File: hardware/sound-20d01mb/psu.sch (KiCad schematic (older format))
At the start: 14 parts

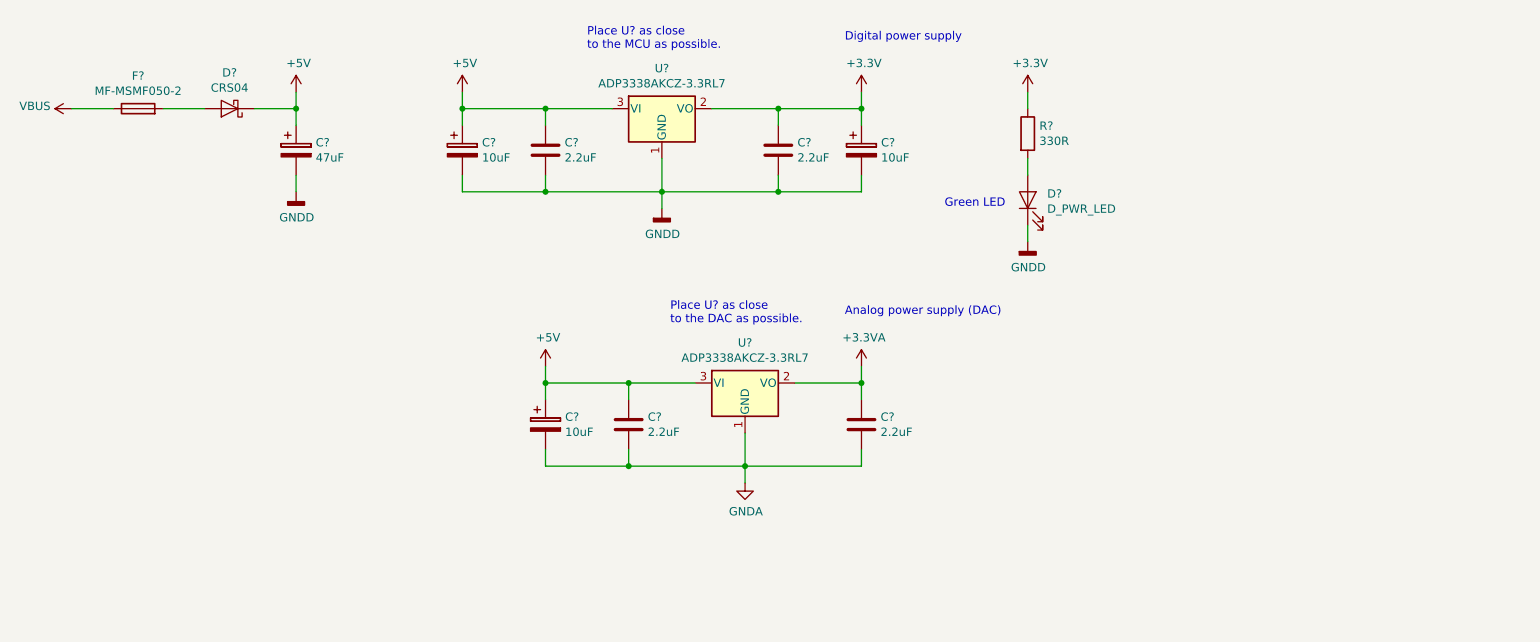
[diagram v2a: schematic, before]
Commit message: Connected GNDD and GNDA
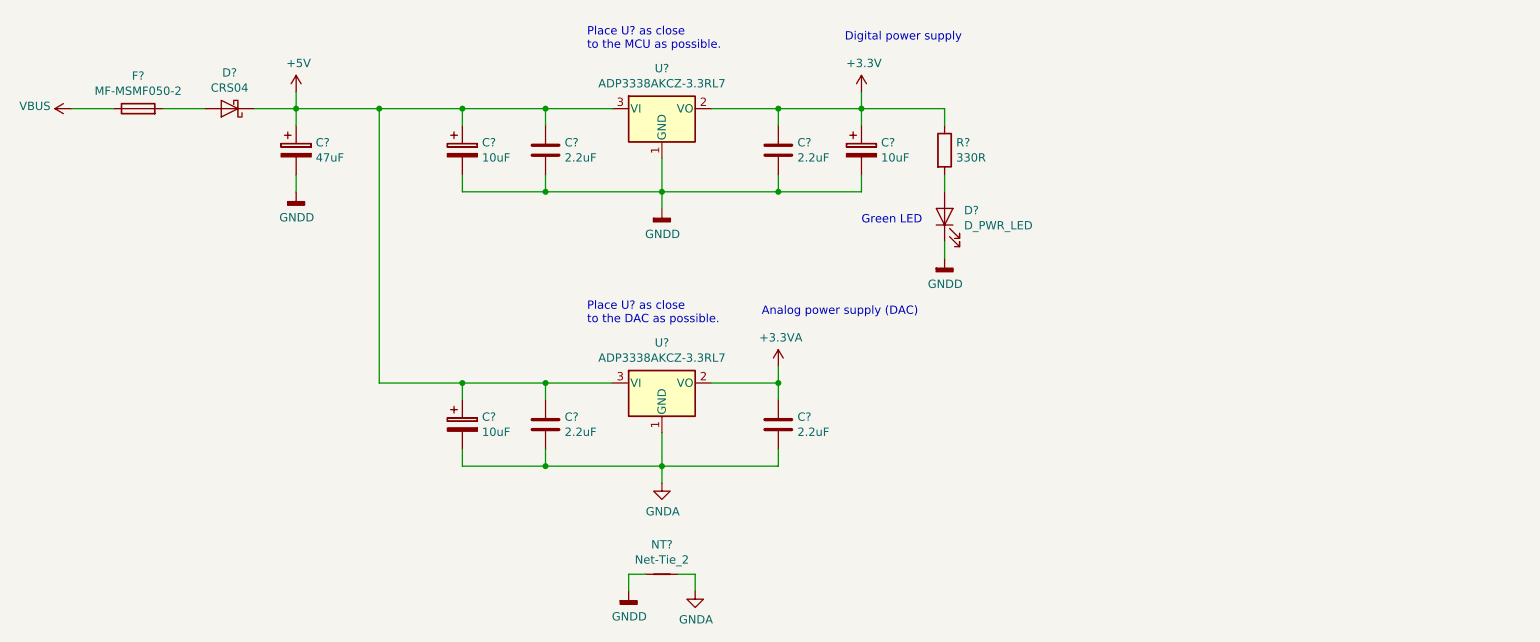
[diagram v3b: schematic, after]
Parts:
- added NT?: Net-Tie_2, NetTie:NetTie-2_SMD_Pad2.0mm, symbol Device:Net-Tie_2
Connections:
- net GNDA: now also NT?.2
- net GNDD: now also NT?.1
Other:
- moved on the sheet: C?, D?, R?, U?
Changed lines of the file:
@@
 L Regulator_Linear:AZ1117-3.3 U?
 U 1 1 60DF628F
-P 6150 4450
-F 0 "U?" H 6150 4692 50  0000 C CNN
-F 1 "ADP3338AKCZ-3.3RL7" H 6150 4601 50  0000 C CNN
-F 2 "Package_TO_SOT_SMD:SOT-223-3_TabPin2" H 6150 4700 50  0001 C CIN
-F 3 "https://www.analog.com/media/en/technical-documentation/data-sheets/adp3338.pdf" H 6150 4450 50  0001 C CNN
-	1    6150 4450
+P 5650 4450
+F 0 "U?" H 5650 4692 50  0000 C CNN
+F 1 "ADP3338AKCZ-3.3RL7" H 5650 4601 50  0000 C CNN
+F 2 "Package_TO_SOT_SMD:SOT-223-3_TabPin2" H 5650 4700 50  0001 C CIN
+F 3 "https://www.analog.com/media/en/technical-documentation/data-sheets/adp3338.pdf" H 5650 4450 50  0001 C CNN
+	1    5650 4450
 	1    0    0    -1
 $EndComp
@@
 L Device:C C?
 U 1 1 60E015B2
-P 6850 4700
+P 6350 4700
 AR Path="/60DE2DF4/60E015B2" Ref="C?"  Part="1"
 AR Path="/60DE2DF1/60E015B2" Ref="C?"  Part="1"
 AR Path="/61033008/60E015B2" Ref="C?"  Part="1"
-F 0 "C?" H 6965 4746 50  0000 L CNN
-F 1 "2.2uF" H 6965 4655 50  0000 L CNN
-F 2 "Capacitor_SMD:C_1206_3216Metric_Pad1.42x1.75mm_HandSolder" H 6888 4550 50  0001 C CNN
-F 3 "~" H 6850 4700 50  0001 C CNN
-	1    6850 4700
+F 0 "C?" H 6465 4746 50  0000 L CNN
+F 1 "2.2uF" H 6465 4655 50  0000 L CNN
+F 2 "Capacitor_SMD:C_1206_3216Metric_Pad1.42x1.75mm_HandSolder" H 6388 4550 50  0001 C CNN
+F 3 "~" H 6350 4700 50  0001 C CNN
+	1    6350 4700
 	1    0    0    -1
 $EndComp
@@
 L Device:C C?
 U 1 1 60E01602
-P 5450 4700
+P 4950 4700
 AR Path="/60DE2DF4/60E01602" Ref="C?"  Part="1"
 AR Path="/60DE2DF1/60E01602" Ref="C?"  Part="1"
 AR Path="/61033008/60E01602" Ref="C?"  Part="1"
-F 0 "C?" H 5565 4746 50  0000 L CNN
-F 1 "2.2uF" H 5565 4655 50  0000 L CNN
-F 2 "Capacitor_SMD:C_1206_3216Metric_Pad1.42x1.75mm_HandSolder" H 5488 4550 50  0001 C CNN
-F 3 "~" H 5450 4700 50  0001 C CNN
-	1    5450 4700
+F 0 "C?" H 5065 4746 50  0000 L CNN
+F 1 "2.2uF" H 5065 4655 50  0000 L CNN
+F 2 "Capacitor_SMD:C_1206_3216Metric_Pad1.42x1.75mm_HandSolder" H 4988 4550 50  0001 C CNN
+F 3 "~" H 4950 4700 50  0001 C CNN
+	1    4950 4700
 	1    0    0    -1
 $EndComp
@@
 L power:GNDA #PWR?
 U 1 1 60E01644
-P 6150 5050
-F 0 "#PWR?" H 6150 4800 50  0001 C CNN
-F 1 "GNDA" H 6155 4877 50  0000 C CNN
-F 2 "" H 6150 5050 50  0001 C CNN
-F 3 "" H 6150 5050 50  0001 C CNN
-	1    6150 5050
-	1    0    0    -1
-$EndComp
-Wire Wire Line
-	6150 4750 6150 4950
+P 5650 5050
+F 0 "#PWR?" H 5650 4800 50  0001 C CNN
+F 1 "GNDA" H 5655 4877 50  0000 C CNN
+F 2 "" H 5650 5050 50  0001 C CNN
+F 3 "" H 5650 5050 50  0001 C CNN
+	1    5650 5050
+	1    0    0    -1
+$EndComp
+Wire Wire Line
+	5650 4750 5650 4950
 $Comp
 L power:+3.3VA #PWR?
 U 1 1 60E017A8
-P 6850 4350
-F 0 "#PWR?" H 6850 4200 50  0001 C CNN
-F 1 "+3.3VA" H 6865 4523 50  0000 C CNN
-F 2 "" H 6850 4350 50  0001 C CNN
-F 3 "" H 6850 4350 50  0001 C CNN
-	1    6850 4350
-	1    0    0    -1
-$EndComp
-Wire Wire Line
-	6850 4850 6850 4950
-Wire Wire Line
-	6150 4950 6150 5050
-Connection ~ 6150 4950
-Wire Wire Line
-	5450 4950 5450 4850
-Wire Wire Line
-	5450 4450 5450 4550
-Text Notes 6750 4050 0    50   ~ 0
+P 6350 4350
+F 0 "#PWR?" H 6350 4200 50  0001 C CNN
+F 1 "+3.3VA" H 6365 4523 50  0000 C CNN
+F 2 "" H 6350 4350 50  0001 C CNN
+F 3 "" H 6350 4350 50  0001 C CNN
+	1    6350 4350
+	1    0    0    -1
+$EndComp
+Wire Wire Line
+	6350 4850 6350 4950
+Wire Wire Line
+	5650 4950 5650 5050
+Connection ~ 5650 4950
+Wire Wire Line
+	4950 4950 4950 4850
+Wire Wire Line
+	4950 4450 4950 4550
+Text Notes 6250 4050 0    50   ~ 0
 Analog power supply (DAC)
 $Comp
@@
 Place U? as close\nto the MCU as possible.
 $Comp
-L power:+5V #PWR?
-U 1 1 613DA71E
-P 4950 4350
-F 0 "#PWR?" H 4950 4200 50  0001 C CNN
-F 1 "+5V" H 4965 4523 50  0000 C CNN
-F 2 "" H 4950 4350 50  0001 C CNN
-F 3 "" H 4950 4350 50  0001 C CNN
-	1    4950 4350
-	1    0    0    -1
-$EndComp
-Wire Wire Line
-	4950 4450 4950 4350
-$Comp
 L Device:CP C?
 U 1 1 613DBAC3
-P 4950 4700
-F 0 "C?" H 5068 4746 50  0000 L CNN
-F 1 "10uF" H 5068 4655 50  0000 L CNN
-F 2 "Capacitor_SMD:CP_Elec_4x5.4" H 4988 4550 50  0001 C CNN
-F 3 "~" H 4950 4700 50  0001 C CNN
-	1    4950 4700
-	1    0    0    -1
-$EndComp
-Wire Wire Line
-	4950 4450 5450 4450
-Wire Wire Line
-	4950 4450 4950 4550
-Connection ~ 4950 4450
-Wire Wire Line
-	4950 4850 4950 4950
-Wire Wire Line
-	4950 4950 5450 4950
-Text Notes 5700 4100 0    50   ~ 0
+P 4450 4700
+F 0 "C?" H 4568 4746 50  0000 L CNN
+F 1 "10uF" H 4568 4655 50  0000 L CNN
+F 2 "Capacitor_SMD:CP_Elec_4x5.4" H 4488 4550 50  0001 C CNN
+F 3 "~" H 4450 4700 50  0001 C CNN
+	1    4450 4700
+	1    0    0    -1
+$EndComp
+Wire Wire Line
+	4450 4450 4450 4550
+Wire Wire Line
+	4450 4850 4450 4950
+Wire Wire Line
+	4450 4950 4950 4950
+Text Notes 5200 4100 0    50   ~ 0
 Place U? as close\nto the DAC as possible.
 $Comp
 L Device:LED D?
 U 1 1 61475539
-P 7850 3350
-F 0 "D?" V 7888 3233 50  0000 R CNN
-F 1 "D_PWR_LED" V 7797 3233 50  0000 R CNN
-F 2 "LED_SMD:LED_1206_3216Metric_Pad1.42x1.75mm_HandSolder" H 7850 3350 50  0001 C CNN
-F 3 "~" H 7850 3350 50  0001 C CNN
-	1    7850 3350
+P 7350 3450
+F 0 "D?" V 7388 3333 50  0000 R CNN
+F 1 "D_PWR_LED" V 7297 3333 50  0000 R CNN
+F 2 "LED_SMD:LED_1206_3216Metric_Pad1.42x1.75mm_HandSolder" H 7350 3450 50  0001 C CNN
+F 3 "~" H 7350 3450 50  0001 C CNN
+	1    7350 3450
 	0    -1   -1   0
 $EndComp
 Wire Wire Line
-	7850 3200 7850 3100
-Wire Wire Line
-	7850 2800 7850 2700
-$Comp
-L power:+3.3V #PWR?
-U 1 1 61475F89
-P 7850 2700
-F 0 "#PWR?" H 7850 2550 50  0001 C CNN
-F 1 "+3.3V" H 7865 2873 50  0000 C CNN
-F 2 "" H 7850 2700 50  0001 C CNN
-F 3 "" H 7850 2700 50  0001 C CNN
-	1    7850 2700
-	1    0    0    -1
-$EndComp
+	7350 3300 7350 3200
+Wire Wire Line
+	7350 2900 7350 2800
 $Comp
 L Device:R R?
 U 1 1 61476045
-P 7850 2950
-F 0 "R?" H 7920 2996 50  0000 L CNN
-F 1 "330R" H 7920 2905 50  0000 L CNN
-F 2 "Resistor_SMD:R_1206_3216Metric_Pad1.42x1.75mm_HandSolder" V 7780 2950 50  0001 C CNN
-F 3 "~" H 7850 2950 50  0001 C CNN
-	1    7850 2950
+P 7350 3050
+F 0 "R?" H 7420 3096 50  0000 L CNN
+F 1 "330R" H 7420 3005 50  0000 L CNN
+F 2 "Resistor_SMD:R_1206_3216Metric_Pad1.42x1.75mm_HandSolder" V 7280 3050 50  0001 C CNN
+F 3 "~" H 7350 3050 50  0001 C CNN
+	1    7350 3050
 	1    0    0    -1
 $EndComp
@@
 L power:GNDD #PWR?
 U 1 1 614762B1
-P 7850 3600
-F 0 "#PWR?" H 7850 3350 50  0001 C CNN
-F 1 "GNDD" H 7854 3445 50  0000 C CNN
-F 2 "" H 7850 3600 50  0001 C CNN
-F 3 "" H 7850 3600 50  0001 C CNN
-	1    7850 3600
-	1    0    0    -1
-$EndComp
-Wire Wire Line
-	7850 3500 7850 3600
+P 7350 3700
+F 0 "#PWR?" H 7350 3450 50  0001 C CNN
+F 1 "GNDD" H 7354 3545 50  0000 C CNN
+F 2 "" H 7350 3700 50  0001 C CNN
+F 3 "" H 7350 3700 50  0001 C CNN
+	1    7350 3700
+	1    0    0    -1
+$EndComp
+Wire Wire Line
+	7350 3600 7350 3700
 Wire Wire Line
 	5950 2800 6350 2800
@@
 Connection ~ 6350 3300
 Wire Wire Line
-	6850 4350 6850 4450
-Wire Wire Line
-	6450 4450 6850 4450
-Connection ~ 6850 4450
-Wire Wire Line
-	6850 4450 6850 4550
-Wire Wire Line
-	6850 4950 6150 4950
+	6350 4350 6350 4450
+Wire Wire Line
+	5950 4450 6350 4450
+Connection ~ 6350 4450
+Wire Wire Line
+	6350 4450 6350 4550
+Wire Wire Line
+	6350 4950 5650 4950
 Wire Wire Line
 	4950 2800 5350 2800
@@
 Connection ~ 4950 3300
 Wire Wire Line
-	5450 4450 5850 4450
-Wire Wire Line
-	6150 4950 5450 4950
-Connection ~ 5450 4450
-Connection ~ 5450 4950
-$Comp
-L power:+5V #PWR?
-U 1 1 6148456A
-P 4450 2700
-F 0 "#PWR?" H 4450 2550 50  0001 C CNN
-F 1 "+5V" H 4465 2873 50  0000 C CNN
-F 2 "" H 4450 2700 50  0001 C CNN
-F 3 "" H 4450 2700 50  0001 C CNN
-	1    4450 2700
-	1    0    0    -1
-$EndComp
-Wire Wire Line
-	4450 2800 4450 2700
-Connection ~ 4450 2800
+	4950 4450 5350 4450
+Wire Wire Line
+	5650 4950 4950 4950
+Connection ~ 4950 4450
+Connection ~ 4950 4950
 $Comp
 L Device:D_Schottky D?
@@
 	-1   0    0    1
 $EndComp
-Text Notes 7350 3400 0    50   ~ 0
+Text Notes 6850 3500 0    50   ~ 0
 Green LED
 $Comp
@@
 Wire Wire Line
 	2350 2800 2100 2800
+Wire Wire Line
+	3450 2800 3950 2800
+Connection ~ 4450 2800
+Wire Wire Line
+	3950 2800 3950 4450
+Connection ~ 3950 2800
+Wire Wire Line
+	3950 2800 4450 2800
+$Comp
+L Device:Net-Tie_2 NT?
+U 1 1 61596519
+P 5650 5600
+F 0 "NT?" H 5650 5778 50  0000 C CNN
+F 1 "Net-Tie_2" H 5650 5687 50  0000 C CNN
+F 2 "NetTie:NetTie-2_SMD_Pad2.0mm" H 5650 5600 50  0001 C CNN
+F 3 "~" H 5650 5600 50  0001 C CNN
+	1    5650 5600
+	1    0    0    -1
+$EndComp
+Wire Wire Line
+	5450 5600 5450 5700
+$Comp
+L power:GNDD #PWR?
+U 1 1 61598760
+P 5450 5700
+F 0 "#PWR?" H 5450 5450 50  0001 C CNN
+F 1 "GNDD" H 5454 5545 50  0000 C CNN
+F 2 "" H 5450 5700 50  0001 C CNN
+F 3 "" H 5450 5700 50  0001 C CNN
+	1    5450 5700
+	1    0    0    -1
+$EndComp
+Wire Wire Line
+	5550 5600 5450 5600
+Wire Wire Line
+	5750 5600 5850 5600
+Wire Wire Line
+	6850 2800 7350 2800
+$Comp
+L power:GNDA #PWR?
+U 1 1 6159AA1F
+P 5850 5700
+F 0 "#PWR?" H 5850 5450 50  0001 C CNN
+F 1 "GNDA" H 5855 5527 50  0000 C CNN
+F 2 "" H 5850 5700 50  0001 C CNN
+F 3 "" H 5850 5700 50  0001 C CNN
+	1    5850 5700
+	1    0    0    -1
+$EndComp
+Wire Wire Line
+	5850 5600 5850 5700
+Wire Wire Line
+	4450 4450 4950 4450
+Wire Wire Line
+	3950 4450 4450 4450
+Connection ~ 4450 4450
 $EndSCHEMATC

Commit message: Updated fuse footprint
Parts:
- F?: footprint (none) -> Fuse:Fuse_1812_4532Metric_Pad1.30x3.40mm_HandSolder
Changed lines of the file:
@@
 F 0 "F?" V 2697 2800 50  0000 C CNN
 F 1 "MF-MSMF050-2" V 2606 2800 50  0000 C CNN
-F 2 "" V 2430 2800 50  0001 C CNN
+F 2 "Fuse:Fuse_1812_4532Metric_Pad1.30x3.40mm_HandSolder" V 2430 2800 50  0001 C CNN
 F 3 "~" H 2500 2800 50  0001 C CNN
 	1    2500 2800

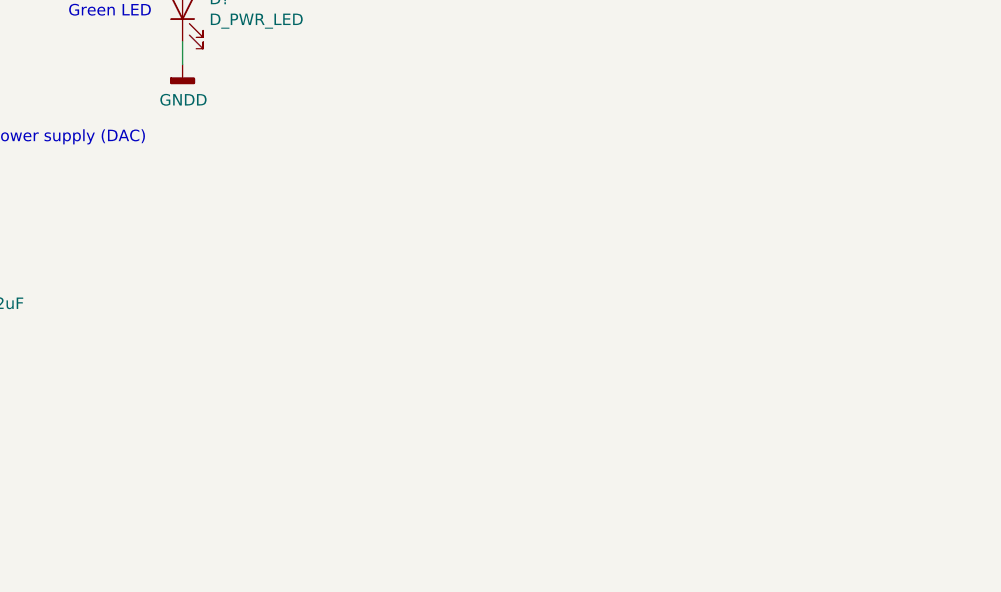
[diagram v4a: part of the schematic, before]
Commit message: Added L7805
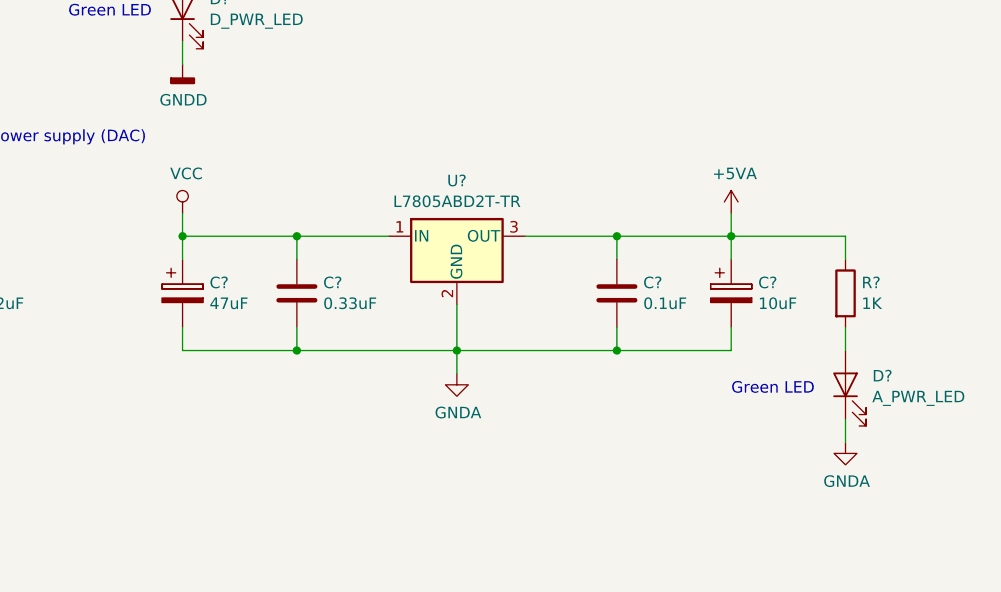
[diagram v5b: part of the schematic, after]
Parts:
- added C?: 0.33uF, Capacitor_SMD:C_1206_3216Metric_Pad1.42x1.75mm_HandSolder, symbol Device:C
- added C?: 0.1uF, Capacitor_SMD:C_1206_3216Metric_Pad1.42x1.75mm_HandSolder, symbol Device:C
- added C?: 10uF, Capacitor_SMD:CP_Elec_4x5.4, symbol Device:CP
- added C?: 47uF, Capacitor_SMD:CP_Elec_6.3x5.4, symbol Device:CP
- added D?: A_PWR_LED, LED_SMD:LED_1206_3216Metric_Pad1.42x1.75mm_HandSolder, symbol Device:LED
- added R?: 1K, Resistor_SMD:R_1206_3216Metric_Pad1.42x1.75mm_HandSolder, symbol Device:R
- added U?: L7805ABD2T-TR, Package_TO_SOT_SMD:TO-263-2, symbol Regulator_Linear:L7805
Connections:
- net GNDA: now also C?.2, C?.2, C?.2, C?.2, D?.1 (K), U?.2 (GND)
- new net: D?.2 (A), R?.2
- new net +5VA: C?.1, C?.1, R?.1, U?.3 (OUT)
- new net VCC: C?.1, C?.1, U?.1 (IN)
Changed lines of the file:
@@
 	3950 4450 4450 4450
 Connection ~ 4450 4450
+$Comp
+L Regulator_Linear:L7805 U?
+U 1 1 619AB518
+P 8550 4450
+F 0 "U?" H 8550 4692 50  0000 C CNN
+F 1 "L7805ABD2T-TR" H 8550 4601 50  0000 C CNN
+F 2 "Package_TO_SOT_SMD:TO-263-2" H 8575 4300 50  0001 L CIN
+F 3 "https://www.st.com/resource/en/datasheet/l78.pdf" H 8550 4400 50  0001 C CNN
+	1    8550 4450
+	1    0    0    -1
+$EndComp
+$Comp
+L Device:C C?
+U 1 1 619AB62A
+P 7850 4700
+F 0 "C?" H 7965 4746 50  0000 L CNN
+F 1 "0.33uF" H 7965 4655 50  0000 L CNN
+F 2 "Capacitor_SMD:C_1206_3216Metric_Pad1.42x1.75mm_HandSolder" H 7888 4550 50  0001 C CNN
+F 3 "~" H 7850 4700 50  0001 C CNN
+	1    7850 4700
+	1    0    0    -1
+$EndComp
+$Comp
+L Device:C C?
+U 1 1 619AB6DE
+P 9250 4700
+F 0 "C?" H 9365 4746 50  0000 L CNN
+F 1 "0.1uF" H 9365 4655 50  0000 L CNN
+F 2 "Capacitor_SMD:C_1206_3216Metric_Pad1.42x1.75mm_HandSolder" H 9288 4550 50  0001 C CNN
+F 3 "~" H 9250 4700 50  0001 C CNN
+	1    9250 4700
+	1    0    0    -1
+$EndComp
+$Comp
+L Device:CP C?
+U 1 1 619AB778
+P 9750 4700
+F 0 "C?" H 9868 4746 50  0000 L CNN
+F 1 "10uF" H 9868 4655 50  0000 L CNN
+F 2 "Capacitor_SMD:CP_Elec_4x5.4" H 9788 4550 50  0001 C CNN
+F 3 "~" H 9750 4700 50  0001 C CNN
+	1    9750 4700
+	1    0    0    -1
+$EndComp
+$Comp
+L Device:CP C?
+U 1 1 619AB88D
+P 7350 4700
+F 0 "C?" H 7468 4746 50  0000 L CNN
+F 1 "47uF" H 7468 4655 50  0000 L CNN
+F 2 "Capacitor_SMD:CP_Elec_6.3x5.4" H 7388 4550 50  0001 C CNN
+F 3 "~" H 7350 4700 50  0001 C CNN
+	1    7350 4700
+	1    0    0    -1
+$EndComp
+$Comp
+L power:GNDA #PWR?
+U 1 1 619AB987
+P 8550 5050
+F 0 "#PWR?" H 8550 4800 50  0001 C CNN
+F 1 "GNDA" H 8555 4877 50  0000 C CNN
+F 2 "" H 8550 5050 50  0001 C CNN
+F 3 "" H 8550 5050 50  0001 C CNN
+	1    8550 5050
+	1    0    0    -1
+$EndComp
+Wire Wire Line
+	8850 4450 9250 4450
+Wire Wire Line
+	7350 4450 7850 4450
+Wire Wire Line
+	7850 4550 7850 4450
+Connection ~ 7850 4450
+Wire Wire Line
+	7850 4450 8250 4450
+Wire Wire Line
+	9250 4550 9250 4450
+Connection ~ 9250 4450
+Wire Wire Line
+	9250 4450 9750 4450
+Wire Wire Line
+	7850 4850 7850 4950
+Wire Wire Line
+	7850 4950 8550 4950
+Wire Wire Line
+	9250 4950 9250 4850
+Wire Wire Line
+	8550 4750 8550 4950
+Connection ~ 8550 4950
+Wire Wire Line
+	8550 4950 9250 4950
+Wire Wire Line
+	8550 4950 8550 5050
+Wire Wire Line
+	7350 4550 7350 4450
+Wire Wire Line
+	9750 4550 9750 4450
+Wire Wire Line
+	9750 4850 9750 4950
+Wire Wire Line
+	9750 4950 9250 4950
+Connection ~ 9250 4950
+Wire Wire Line
+	7850 4950 7350 4950
+Wire Wire Line
+	7350 4950 7350 4850
+Connection ~ 7850 4950
+$Comp
+L power:+5VA #PWR?
+U 1 1 619CBAE2
+P 9750 4350
+AR Path="/60DE2DF4/619CBAE2" Ref="#PWR?"  Part="1"
+AR Path="/61033008/619CBAE2" Ref="#PWR?"  Part="1"
+F 0 "#PWR?" H 9750 4200 50  0001 C CNN
+F 1 "+5VA" H 9765 4523 50  0000 C CNN
+F 2 "" H 9750 4350 50  0001 C CNN
+F 3 "" H 9750 4350 50  0001 C CNN
+	1    9750 4350
+	1    0    0    -1
+$EndComp
+Wire Wire Line
+	9750 4450 9750 4350
+Connection ~ 9750 4450
+$Comp
+L power:VCC #PWR?
+U 1 1 619CEE4C
+P 7350 4350
+AR Path="/619CEE4C" Ref="#PWR?"  Part="1"
+AR Path="/61033008/619CEE4C" Ref="#PWR?"  Part="1"
+F 0 "#PWR?" H 7350 4200 50  0001 C CNN
+F 1 "VCC" H 7367 4523 50  0000 C CNN
+F 2 "" H 7350 4350 50  0001 C CNN
+F 3 "" H 7350 4350 50  0001 C CNN
+	1    7350 4350
+	1    0    0    -1
+$EndComp
+Wire Wire Line
+	7350 4450 7350 4350
+Connection ~ 7350 4450
+$Comp
+L Device:LED D?
+U 1 1 619D82C7
+P 10250 5100
+F 0 "D?" V 10288 4983 50  0000 R CNN
+F 1 "A_PWR_LED" V 10197 4983 50  0000 R CNN
+F 2 "LED_SMD:LED_1206_3216Metric_Pad1.42x1.75mm_HandSolder" H 10250 5100 50  0001 C CNN
+F 3 "~" H 10250 5100 50  0001 C CNN
+	1    10250 5100
+	0    -1   -1   0
+$EndComp
+Wire Wire Line
+	10250 4950 10250 4850
+Wire Wire Line
+	10250 4550 10250 4450
+$Comp
+L Device:R R?
+U 1 1 619D82CF
+P 10250 4700
+F 0 "R?" H 10320 4746 50  0000 L CNN
+F 1 "1K" H 10320 4655 50  0000 L CNN
+F 2 "Resistor_SMD:R_1206_3216Metric_Pad1.42x1.75mm_HandSolder" V 10180 4700 50  0001 C CNN
+F 3 "~" H 10250 4700 50  0001 C CNN
+	1    10250 4700
+	1    0    0    -1
+$EndComp
+Wire Wire Line
+	10250 5250 10250 5350
+Text Notes 9750 5150 0    50   ~ 0
+Green LED
+Wire Wire Line
+	9750 4450 10250 4450
+$Comp
+L power:GNDA #PWR?
+U 1 1 619E1D00
+P 10250 5350
+F 0 "#PWR?" H 10250 5100 50  0001 C CNN
+F 1 "GNDA" H 10255 5177 50  0000 C CNN
+F 2 "" H 10250 5350 50  0001 C CNN
+F 3 "" H 10250 5350 50  0001 C CNN
+	1    10250 5350
+	1    0    0    -1
+$EndComp
 $EndSCHEMATC
